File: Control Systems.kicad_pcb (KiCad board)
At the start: 4 copper layers, 118 parts, among them J1 XT60-M, J10 Battery input, J11 Canbus, J12 Conn_02x03_Odd_Even, J13 USB_RX/TX, J14 Conn_01x08_Socket, J15 Conn_01x08_Socket, J16 Conn_01x03_Pin, J2 10118194-0001LF, J2 47346-0001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

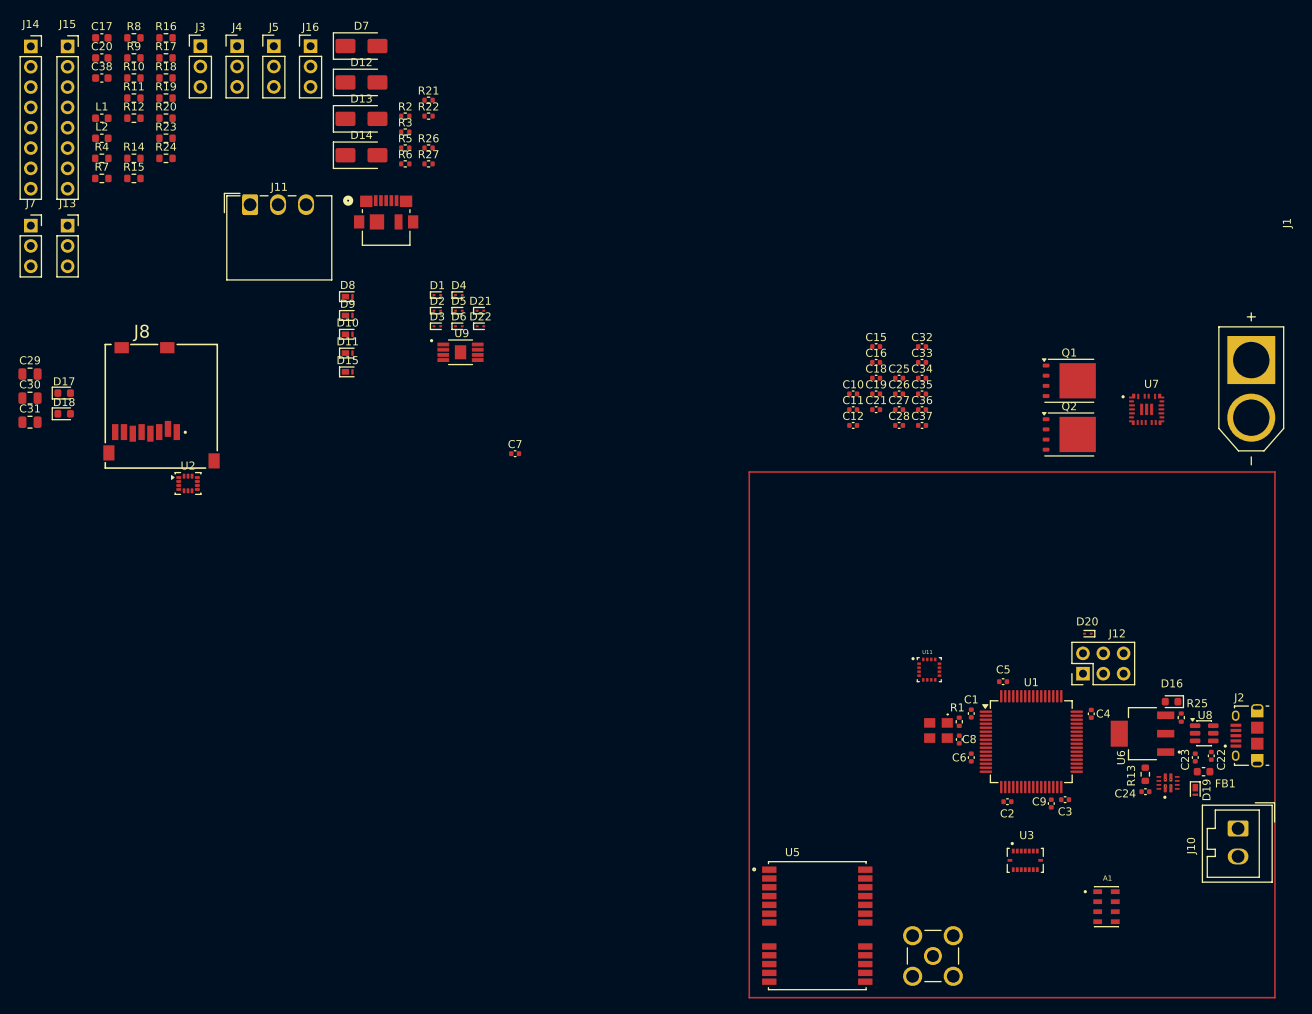
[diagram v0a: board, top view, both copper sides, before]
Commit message: Placement of components and initial VIA placement
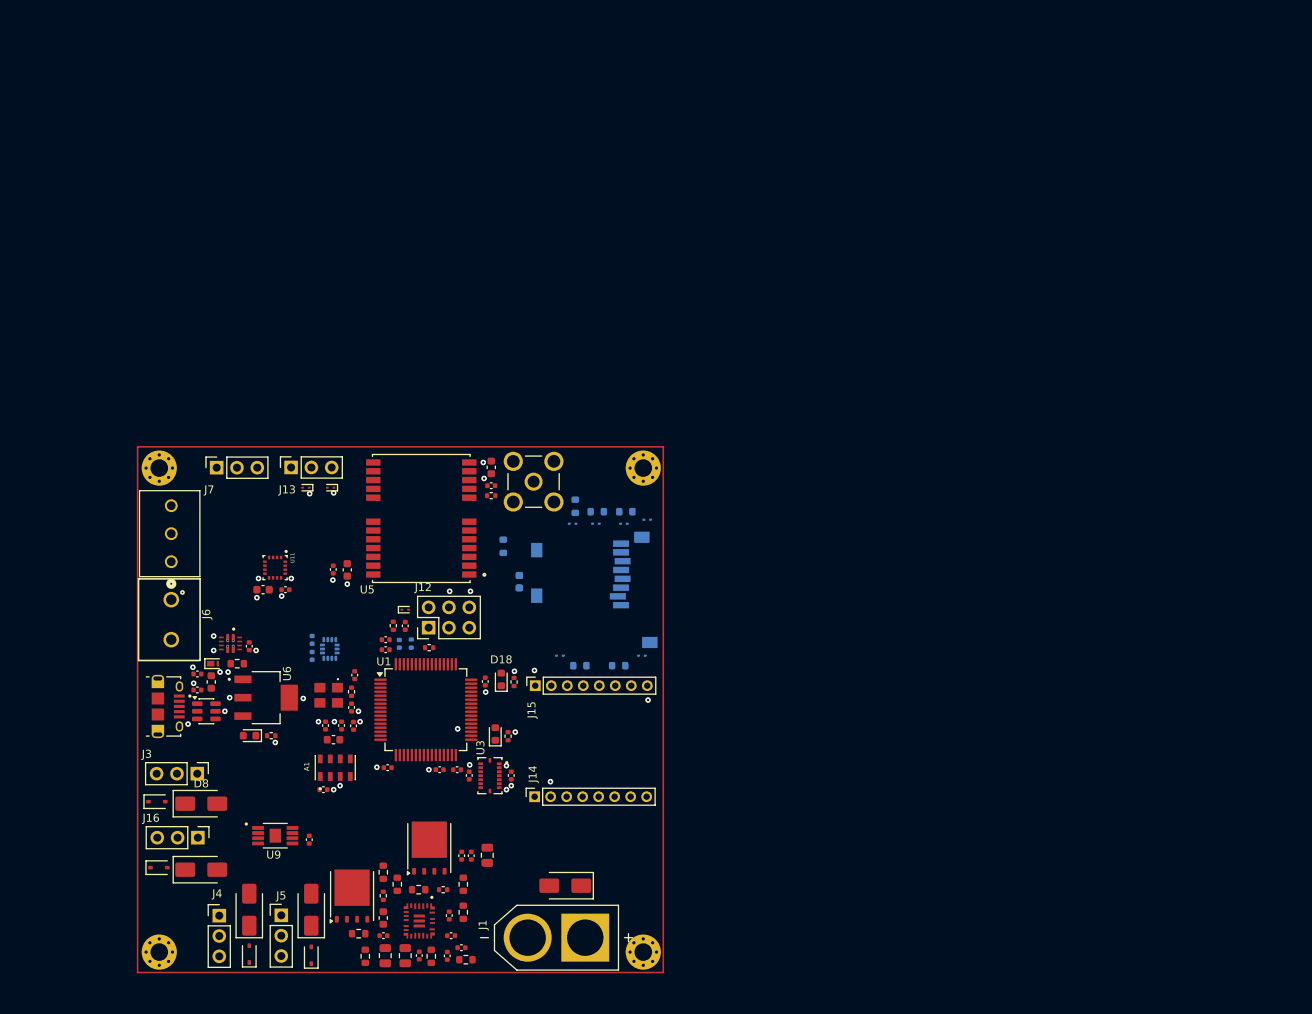
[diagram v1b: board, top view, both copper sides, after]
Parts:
- removed C6: 100n, Capacitor_SMD:C_0402_1005Metric
- removed D15: TVS, Diode_SMD:Nexperia_DSN1608-2_1.6x0.8mm
- removed J11: Canbus, Connector_Wago:Wago_734-163_1x03_P3.50mm_Horizontal
- removed the J2 at (86.4, 37.0)
- removed the J2 at (195.2, 101.2)
- added C13: 1u, Capacitor_SMD:C_0402_1005Metric, F.Cu at (80.8, 100.0)
- added C14: 100n, Capacitor_SMD:C_0402_1005Metric, F.Cu at (82.3, 100.0)
- added C39: 1u, Capacitor_SMD:C_0402_1005Metric, F.Cu at (78.8, 100.0)
- added D23: SD05_SOD323, Diode_SMD:D_SOD-323, F.Cu at (58.0, 117.8)
- added FB2: 120R, Inductor_SMD:L_0603_1608Metric, F.Cu at (79.8, 101.8)
- added J2: 10118194-0001LF, imports:AMPHENOL_10118194-0001LF, F.Cu at (57.8, 97.6)
- added J6: Battery input, imports:691137710002, F.Cu at (59.5, 86.8)
- added MH1: M2, MountingHole:MountingHole_2.2mm_M2_Pad_Via, F.Cu at (58.0, 67.8)
- added MH2: M2, MountingHole:MountingHole_2.2mm_M2_Pad_Via, F.Cu at (58.0, 128.3)
- added MH3: M2, MountingHole:MountingHole_2.2mm_M2_Pad_Via, F.Cu at (118.5, 128.3)
- added MH4: M2, MountingHole:MountingHole_2.2mm_M2_Pad_Via, F.Cu at (118.5, 67.8)
- C15, C16, C20, D1, D2, D3, D4, D5, D6, J8, R10, R11, R12, R5, R7, R8, R9, U2: moved to B.Cu
- D10, D8, D9: value TVS -> SMAJ12A; footprint Diode_SMD:Nexperia_DSN1608-2_1.6x0.8mm -> Diode_SMD:D_SMA
- D11: value TVS -> SMAJ9.0A; footprint Diode_SMD:Nexperia_DSN1608-2_1.6x0.8mm -> Diode_SMD:D_SMA
- D12, D13, D7: value SMAJ6.0CA -> SD05_SOD323; footprint Diode_SMD:D_SMA -> Diode_SMD:D_SOD-323
- D14: value SMAJ6.0CA -> SMAJ12A
- J10: value Battery input -> Canbus; footprint Connector_Wago:Wago_734-132_1x02_P3.50mm_Vertical -> imports:CONN_SD-39357-001_03P_MOL
- J14, J15: footprint Connector_PinSocket_2.54mm:PinSocket_1x08_P2.54mm_Vertical -> Connector_PinSocket_2.00mm:PinSocket_1x08_P2.00mm_Vertical
- J7: value USB_RX/TX -> GPIO
- R4: value 47k -> 4k7; footprint Resistor_SMD:R_0603_1608Metric -> Capacitor_SMD:C_0402_1005Metric; moved to B.Cu
- moved J10 137.5 mm to (59.5, 79.5), turned to 90 degrees
- moved C22 127.0 mm to (62.8, 95.5), turned to 180 degrees
- moved C23 125.2 mm to (62.8, 93.5), turned to 180 degrees
- moved U8 124.8 mm to (63.9, 98.2)
- moved FB1 124.5 mm to (64.5, 94.5), turned to 90 degrees
- moved D19 123.8 mm to (64.7, 92.2), turned to 0 degrees
- moved R16 121.2 mm to (96.3, 129.2)
- moved U10 118.5 mm to (66.9, 89.7), turned to -90 degrees
- moved D16 115.3 mm to (69.3, 101.2)
- moved R17 115.0 mm to (83.8, 128.8), turned to 90 degrees
- moved R13 114.3 mm to (67.8, 92.2), turned to 180 degrees
- moved R25 113.8 mm to (72.0, 101.2), turned to 0 degrees
- moved C24 113.5 mm to (69.2, 90.1), turned to -90 degrees
- moved J14 113.0 mm to (104.9, 108.9), turned to 90 degrees
- moved U7 111.2 mm to (90.5, 124.4), turned to -90 degrees
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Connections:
- net Net-(Q2-D) renamed /SWR_SW1
- net Net-(U5-VCC_RF) renamed /VCC_RF
- D11 pad 1: /Servo +8.2V -> /VIN_7.4V
- D12 pad 1: /PWM_TIM3_CH2 -> /PWM_TIM3_CH3
- D13 pad 1: /PWM_TIM3_CH3 -> /PWM_TIM3_CH4
- D14 pad 1: /PWM_TIM3_CH4 -> /Servo +8.2V
- D17 pad 2: /GP_LED -> /GP_LED_IO
- D18 pad 2: /RX_LED -> /RX_LED_GP
- D19 pad 1: Net-(D19-K) -> /Batt_out
- D21 pad 2: /USART1_RX -> /USART1_TX
- D7 pad 1: /PWM_TIM3_CH1 -> /PWM_TIM3_CH2
- J10 pad 1: GND -> /CAN2_RX
- J10 pad 2: Net-(D19-K) -> /CAN2_TX
- J12 pad 1: /SYS_SWDIO -> /MCU_NRST
- J12 pad 5: /MCU_NRST -> /SYS_SWDIO
- J13 pad 1: /USART1_RX -> /USART1_TX
- J15 pad 5: /SPI1_CS_2 -> /SPI1_CS_3
- R3 pad 1: GND -> /MCU_NRST
- U1 pad 13: +3.3V -> +3.3VA
- U1 pad 36: /GP_LED -> /GP_LED_IO
- U1 pad 50: /RX_LED -> /RX_LED_GP
- U1 pad 58: /USART1_RX -> /USART1_TX
- U10 pad 7: Net-(D19-K) -> /Batt_out
- U10 pad 7_1: Net-(D19-K) -> /Batt_out
- U3 pad 5: /SPI1_CS_3 -> /SPI1_CS_2
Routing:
- net GND: vias 0 -> 20
- net (no net): vias 0 -> 23
- added copper zone on In2.Cu, net +3.3V
- added copper zone on In2.Cu, net +8.2V
- added copper zone on In1.Cu, net GND

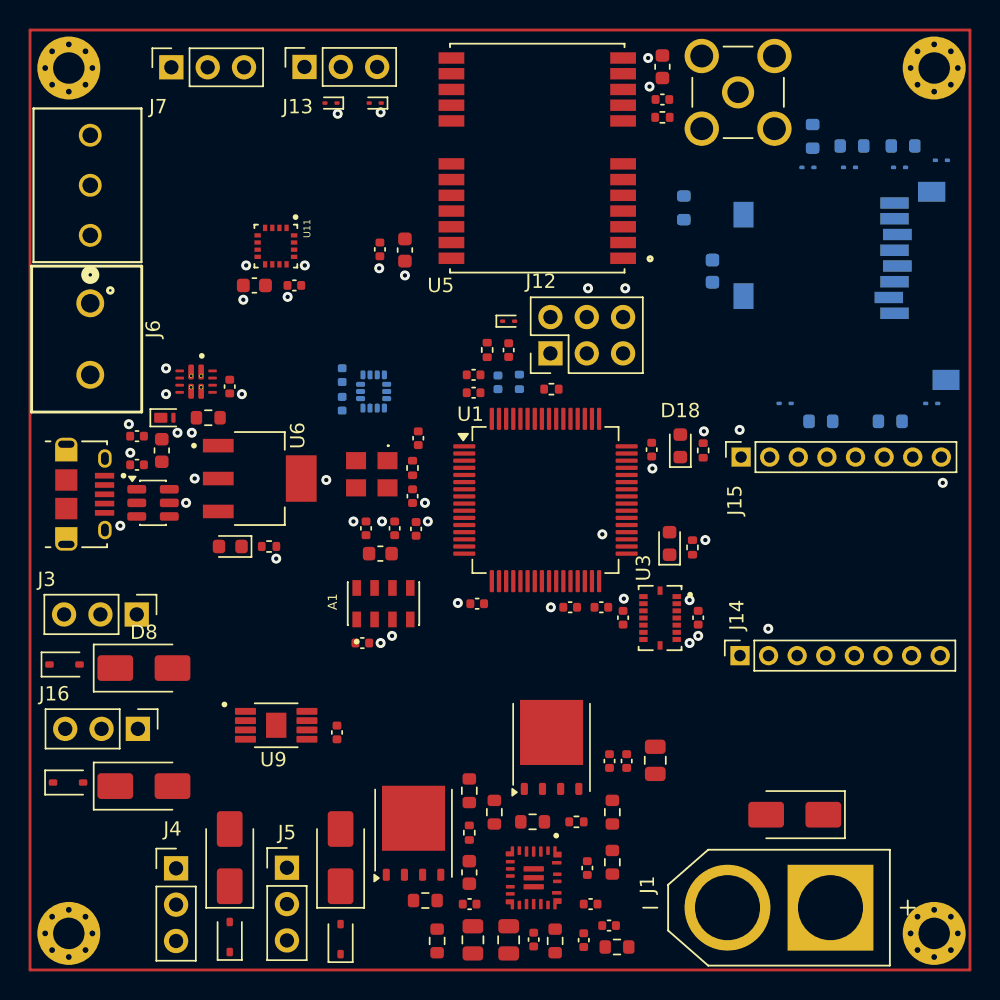
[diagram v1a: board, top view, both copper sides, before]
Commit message: Feat: VIAs placed and some routing
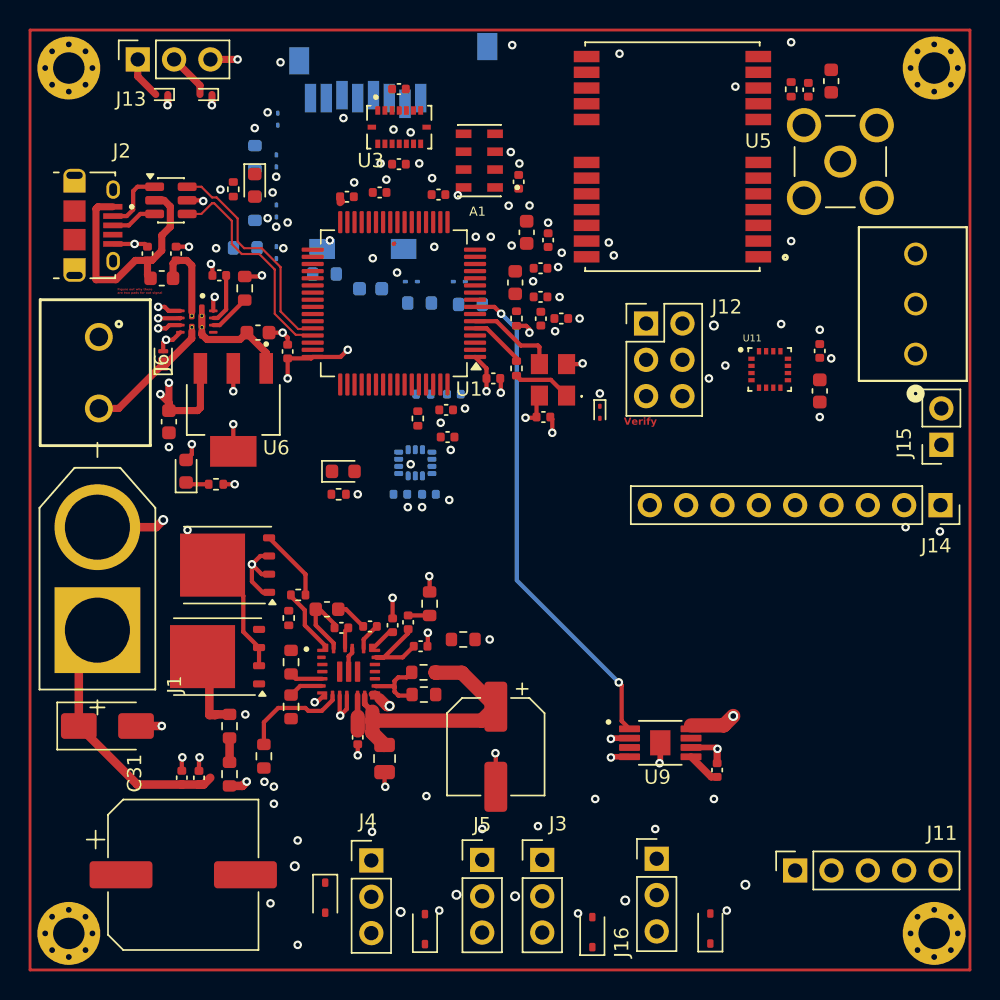
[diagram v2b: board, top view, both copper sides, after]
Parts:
- removed D10, D14, D8, D9: SMAJ12A, Diode_SMD:D_SMA
- removed J7: GPIO, Connector_PinSocket_2.54mm:PinSocket_1x03_P2.54mm_Vertical
- added C40: 10u, Capacitor_SMD:C_0603_1608Metric, F.Cu at (65.0, 92.5)
- added C6: 10u, Capacitor_SMD:C_0603_1608Metric, F.Cu at (71.2, 86.3)
- added J11: Conn_01x05_Socket, Connector_PinSocket_2.54mm:PinSocket_1x05_P2.54mm_Vertical, F.Cu at (108.8, 123.9)
- C30: footprint Capacitor_SMD:C_0805_2012Metric -> Capacitor_SMD:CP_Elec_6.3x5.9
- C31: footprint Capacitor_SMD:C_0805_2012Metric -> Capacitor_SMD:CP_Elec_10x12.6
- J14: value Conn_01x08_Socket -> Conn_01x09_Socket; footprint Connector_PinSocket_2.00mm:PinSocket_1x08_P2.00mm_Vertical -> Connector_PinSocket_2.54mm:PinSocket_1x09_P2.54mm_Vertical
- J15: value Conn_01x08_Socket -> GPIO; footprint Connector_PinSocket_2.00mm:PinSocket_1x08_P2.00mm_Vertical -> Connector_PinSocket_2.54mm:PinSocket_1x02_P2.54mm_Vertical
- moved J10 58.3 mm to (117.2, 87.8)
- moved J1 52.9 mm to (60.0, 103.5), turned to 90 degrees
- moved D11 48.4 mm to (60.7, 113.8), turned to 0 degrees
- moved D1 46.5 mm to (72.6, 71.4), turned to -90 degrees
- moved D23 46.0 mm to (102.8, 128.0), turned to 90 degrees
- moved R7 45.3 mm to (71.0, 74.0), turned to -90 degrees
- moved D2 43.6 mm to (72.5, 74.3), turned to 90 degrees
- moved C11 42.5 mm to (81.1, 69.3), turned to 0 degrees
- moved R10 42.0 mm to (71.0, 77.6), turned to -90 degrees
- moved D7 41.4 mm to (94.6, 128.2), turned to 90 degrees
- moved R26 40.7 mm to (69.5, 76.3), turned to -90 degrees
- moved R11 40.4 mm to (70.3, 80.4), turned to 0 degrees
- moved C38 40.2 mm to (110.5, 90.4), turned to -90 degrees
- moved D5 40.2 mm to (72.5, 77.8), turned to 90 degrees
- moved U3 38.9 mm to (81.1, 71.9), turned to 0 degrees
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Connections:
- J14 pad 1: unconnected-(J14-Pin_1-Pad1) -> +3.3V
- J14 pad 3: unconnected-(J14-Pin_3-Pad3) -> /RADIO_EN
- J14 pad 4: /RADIO_D4 -> /RADIO_D0
- J14 pad 5: +3.3V -> /SPI1_SCK
- J14 pad 6: /RADIO_D0 -> /SPI1_MISO
- J14 pad 7: unconnected-(J14-Pin_7-Pad7) -> /SPI1_MOSI
- J14 pad 8: unconnected-(J14-Pin_8-Pad8) -> /SPI1_CS_3
- J15 pad 1: GND -> /GPIO_1
- J15 pad 2: /SPI1_MISO -> /GPIO_2
- U1 pad 11: /GPIO_1 -> /RADIO_EN
- U1 pad 35: /GPIO_3 -> /GPIO_2
- U1 pad 57: /GPIO_2 -> /GPIO_1
- U8 pad 1: Net-(J2-D+) -> Net-(J2-D-)
- U8 pad 3: Net-(J2-D-) -> Net-(J2-D+)
- U8 pad 4: /USB_D_N -> /USB_D_P
- U8 pad 6: /USB_D_P -> /USB_D_N
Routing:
- net GND: track 0.00 -> 61.9 mm, vias 20 -> 99
- net /Servo_HS_Sw: track 0.00 -> 34.8 mm, vias 0 -> 2
- net +8.2V: track 0.00 -> 26.3 mm, vias 0 -> 8
- net /VIN_7.4V: track 0.00 -> 24.0 mm
- net +3.3V: track 0.00 -> 22.3 mm, vias 0 -> 30
- net +VBUS: track 0.00 -> 17.6 mm
- net /USB_D_N: track 0.00 -> 15.7 mm
- net /USB_D_P: track 0.00 -> 15.7 mm
- net /SWR_SW1: track 0.00 -> 13.7 mm
- net /Batt_out: track 0.00 -> 9.03 mm
- net Net-(U6-IN): track 0.00 -> 7.57 mm
- net Net-(U7-FSW): track 0.00 -> 7.51 mm
- net /MCU_OSC_OUT: track 0.00 -> 6.45 mm
- net Net-(U7-COMP): track 0.00 -> 6.22 mm
- net +VBUSF: track 0.00 -> 5.83 mm
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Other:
- board text added: "Figure out why there are two pads for out signal"
- board text added: "Verify"
